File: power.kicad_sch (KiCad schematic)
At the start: 56 parts, among them J11 Conn_01x02_Pin, J13 Conn_01x02_Pin, J14 Conn_01x02_Pin, J15 Conn_01x02_Pin, J8 Conn_01x02_Pin, U10 MAX4995AAUT, U11 MAX4995AAUT, U35 MAX4995AAUT, U36 TPS7A5201QRGRRQ1, U4 TPSM828302ARDSR, U6 STWD100NYWY3F, U8 MP5073GG-P, U9 MAX4995AAUT

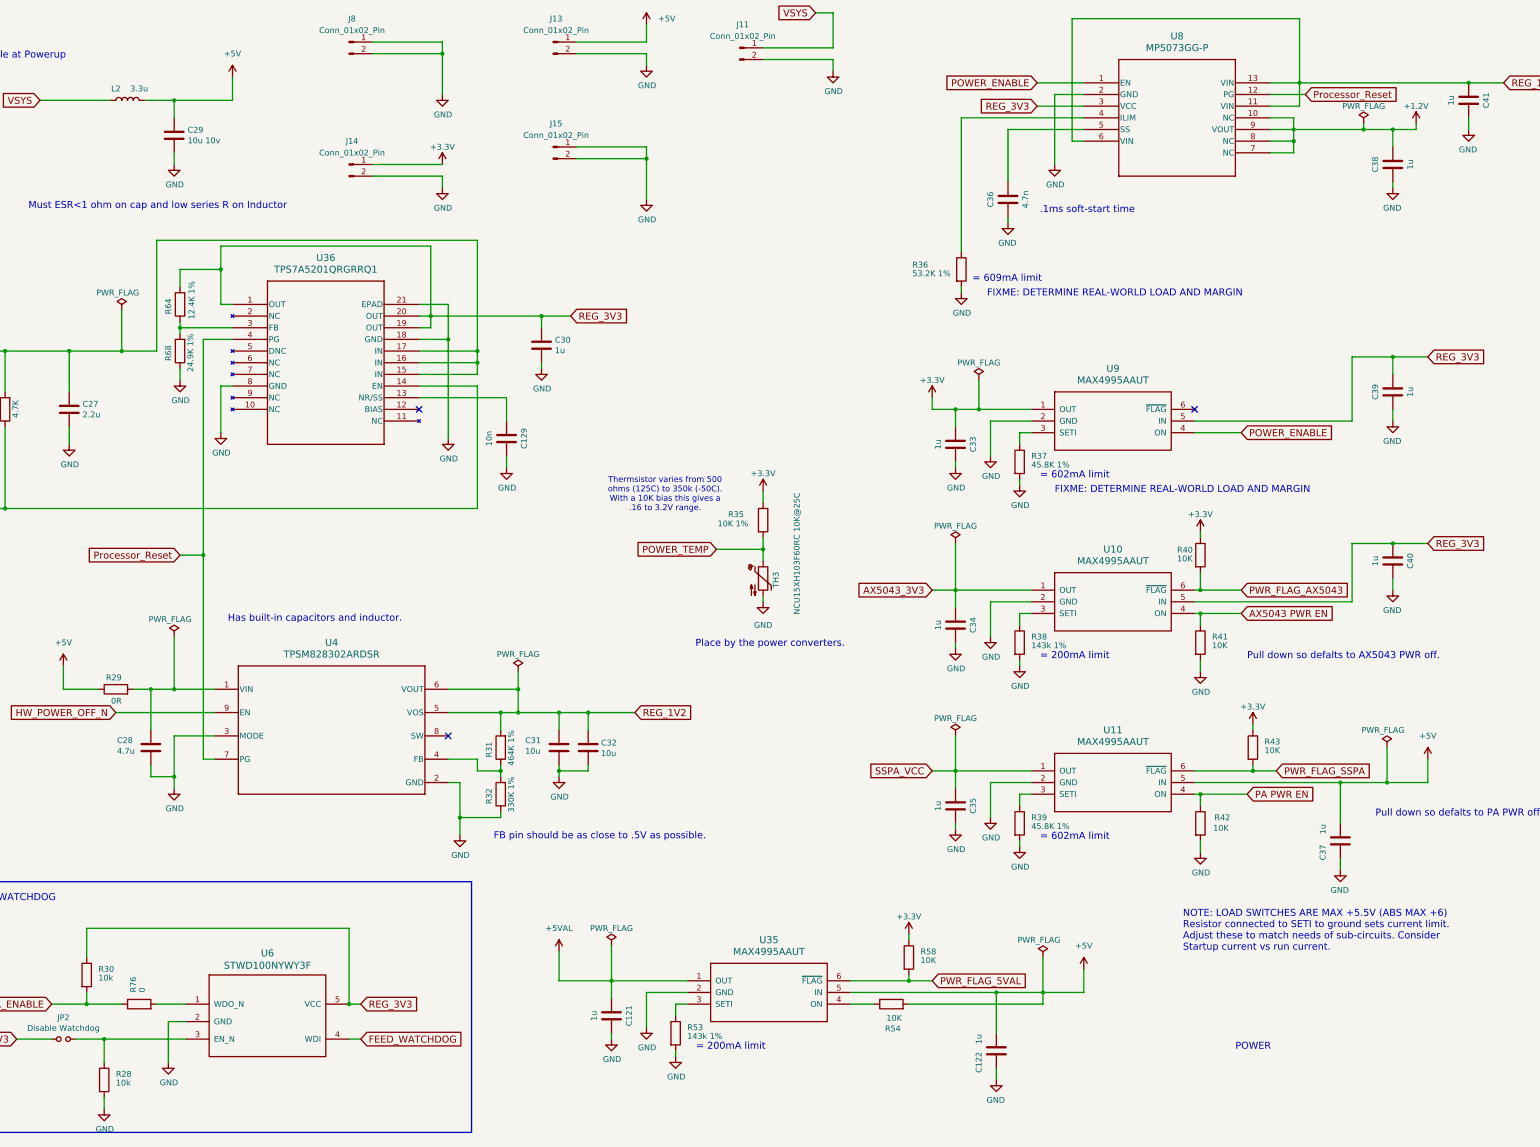
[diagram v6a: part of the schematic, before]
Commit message: Lots of updates to ease manufacturing
Component changes, changes in the formatting of the values, etc.

Signed-off-by: Corey Minyard <corey@minyard.net>
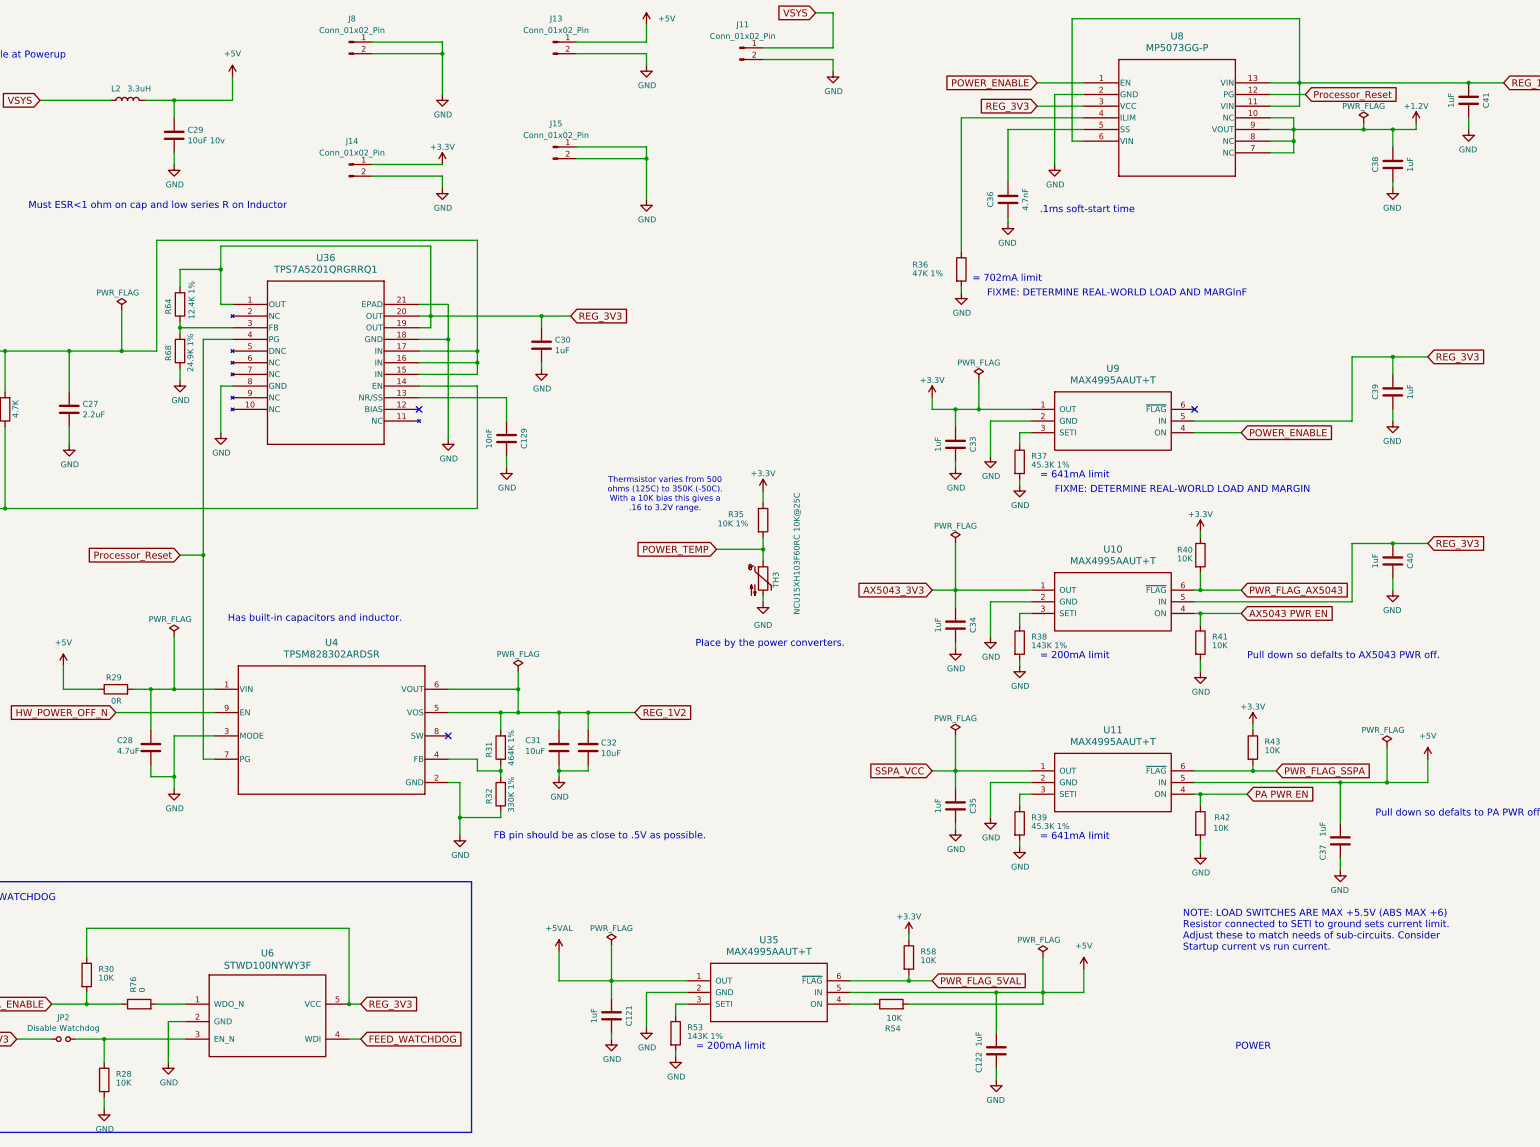
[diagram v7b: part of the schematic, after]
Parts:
- C121, C122, C30, C33, C34, C35, C37, C38, C39, C40, C41: value 1u -> 1uF
- C129: value 10n -> 10nF
- C27: value 2.2u -> 2.2uF
- C28: value 4.7u -> 4.7uF
- C29: value 10u 10v -> 10uF 10v
- C31, C32: value 10u -> 10uF
- C36: value 4.7n -> 4.7nF
- L2: value 3.3u -> 3.3uH
- R28, R30: value 10k -> 10K
- R36: value 53.2K 1% -> 47K 1%
- R37, R39: value 45.8K 1% -> 45.3K 1%
- R38, R53: value 143k 1% -> 143K 1%
- U10, U11, U35, U9: value MAX4995AAUT -> MAX4995AAUT+T
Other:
- note added: "= 641mA limit"
- note added: "= 702mA limit"
- note added: "FIXME: DETERMINE REAL-WORLD LOAD AND MARGInF"
- note added: "Thermsistor varies from 500 ohms (125C) to 350K (-50C). With a 10K bias this gives a .16 to 3.2V range."
- note removed: "= 602mA limit"
- note removed: "= 609mA limit"
- note removed: "Thermsistor varies from 500 ohms (125C) to 350k (-50C). With a 10K bias this gives a .16 to 3.2V range."
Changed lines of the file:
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@@
 		)
 	)
-	(text "Thermsistor varies from 500\nohms (125C) to 350k (-50C).\nWith a 10K bias this gives a\n.16 to 3.2V range."
+	(text "Thermsistor varies from 500\nohms (125C) to 350K (-50C).\nWith a 10K bias this gives a\n.16 to 3.2V range."
 		(exclude_from_sim no)
 		(at 209.804 123.952 0)
@@
 		)
 	)
-	(text "FIXME: DETERMINE REAL-WORLD LOAD AND MARGIN"
+	(text "FIXME: DETERMINE REAL-WORLD LOAD AND MARGInF"
 		(exclude_from_sim no)
 		(at 279.908 81.026 0)
@@
 		)
 	)
-	(text "= 602mA limit"
+	(text "= 641mA limit"
 		(exclude_from_sim no)
 		(at 291.465 120.65 0)
@@
 		)
 	)
-	(text "= 609mA limit"
+	(text "= 702mA limit"
 		(exclude_from_sim no)
 		(at 276.733 77.851 0)
@@
 		)
 	)
-	(text "= 602mA limit"
+	(text "= 641mA limit"
 		(exclude_from_sim no)
 		(at 291.465 199.39 0)
@@
 			)
 		)
-		(property "Value" "1u"
+		(property "Value" "1uF"
 			(at 185.801 92.583 0)
 			(effects
@@
 			)
 		)
-		(property "Value" "2.2u"
+		(property "Value" "2.2uF"
 			(at 82.931 106.553 0)
 			(effects
@@
 			)
 		)
-		(property "Value" "1u"
+		(property "Value" "1uF"
 			(at 364.49 138.43 90)
 			(effects
@@
 			)
 		)
-		(property "Value" "1u"
+		(property "Value" "1uF"
 			(at 353.06 196.85 90)
 			(effects
@@
 			)
 		)
-		(property "Value" "143k 1%"
+		(property "Value" "143K 1%"
 			(at 289.56 156.845 0)
 			(effects
@@
 			)
 		)
-		(property "Value" "45.8K 1%"
+		(property "Value" "45.3K 1%"
 			(at 289.56 196.215 0)
 			(effects
@@
 			)
 		)
-		(property "Value" "1u"
+		(property "Value" "1uF"
 			(at 269.24 152.4 90)
 			(effects
@@
 			)
 		)
-		(property "Value" "1u"
+		(property "Value" "1uF"
 			(at 269.24 191.77 90)
 			(effects
@@
 			)
 		)
-		(property "Value" "1u"
+		(property "Value" "1uF"
 			(at 372.11 101.6 90)
 			(effects
@@
 			)
 		)
-		(property "Value" "1u"
+		(property "Value" "1uF"
 			(at 269.24 113.03 90)
 			(effects
@@
 			)
 		)
-		(property "Value" "45.8K 1%"
+		(property "Value" "45.3K 1%"
 			(at 289.56 117.475 0)
 			(effects
@@
 			)
 		)
-		(property "Value" "1u"
+		(property "Value" "1uF"
 			(at 381 38.1 90)
 			(effects
@@
 			)
 		)
-		(property "Value" "1u"
+		(property "Value" "1uF"
 			(at 372.11 52.07 90)
 			(effects
@@
 			)
 		)
-		(property "Value" "53.2K 1%"
+		(property "Value" "47K 1%"
 			(at 263.652 75.819 0)
 			(effects
@@
 			)
 		)
-		(property "Value" "10k"
+		(property "Value" "10K"
 			(at 86.36 229.235 0)
 			(effects
@@
 			)
 		)
-		(property "Value" "10k"
+		(property "Value" "10K"
 			(at 90.17 252.095 0)
 			(effects
@@
 			)
 		)
-		(property "Value" "10u"
+		(property "Value" "10uF"
 			(at 195.834 180.34 0)
 			(effects
@@
 			)
 		)
-		(property "Value" "10n"
+		(property "Value" "10nF"
 			(at 171.45 111.76 90)
 			(effects
@@
 			)
 		)
-		(property "Value" "3.3u"
+		(property "Value" "3.3uH"
 			(at 95.25 35.56 90)
 			(effects
@@
 			)
 		)
-		(property "Value" "10u 10v"
+		(property "Value" "10uF 10v"
 			(at 105.791 46.863 0)
 			(effects
@@
 			)
 		)
-		(property "Value" "4.7u"
+		(property "Value" "4.7uF"
 			(at 90.424 179.832 0)
 			(effects
@@
 			)
 		)
-		(property "Value" "MAX4995AAUT"
+		(property "Value" "MAX4995AAUT+T"
 			(at 307.34 177.8 0)
 			(effects
@@
 			)
 		)
-		(property "Value" "MAX4995AAUT"
+		(property "Value" "MAX4995AAUT+T"
 			(at 307.34 138.43 0)
 			(effects
@@
 			)
 		)
-		(property "Value" "MAX4995AAUT"
+		(property "Value" "MAX4995AAUT+T"
 			(at 307.34 99.06 0)
 			(effects
@@
 			)
 		)
-		(property "Value" "1u"
+		(property "Value" "1uF"
 			(at 194.31 237.49 90)
 			(effects
@@
 			)
 		)
-		(property "Value" "1u"
+		(property "Value" "1uF"
 			(at 278.13 242.57 90)
 			(effects
@@
 			)
 		)
-		(property "Value" "MAX4995AAUT"
+		(property "Value" "MAX4995AAUT+T"
 			(at 232.41 223.52 0)
 			(effects
@@
 			)
 		)
-		(property "Value" "10u"
+		(property "Value" "10uF"
 			(at 179.324 179.832 0)
 			(effects
@@
 			)
 		)
-		(property "Value" "143k 1%"
+		(property "Value" "143K 1%"
 			(at 214.63 241.935 0)
 			(effects
@@
 			)
 		)
-		(property "Value" "4.7n"
+		(property "Value" "4.7nF"
 			(at 288.29 59.69 90)
 			(effects

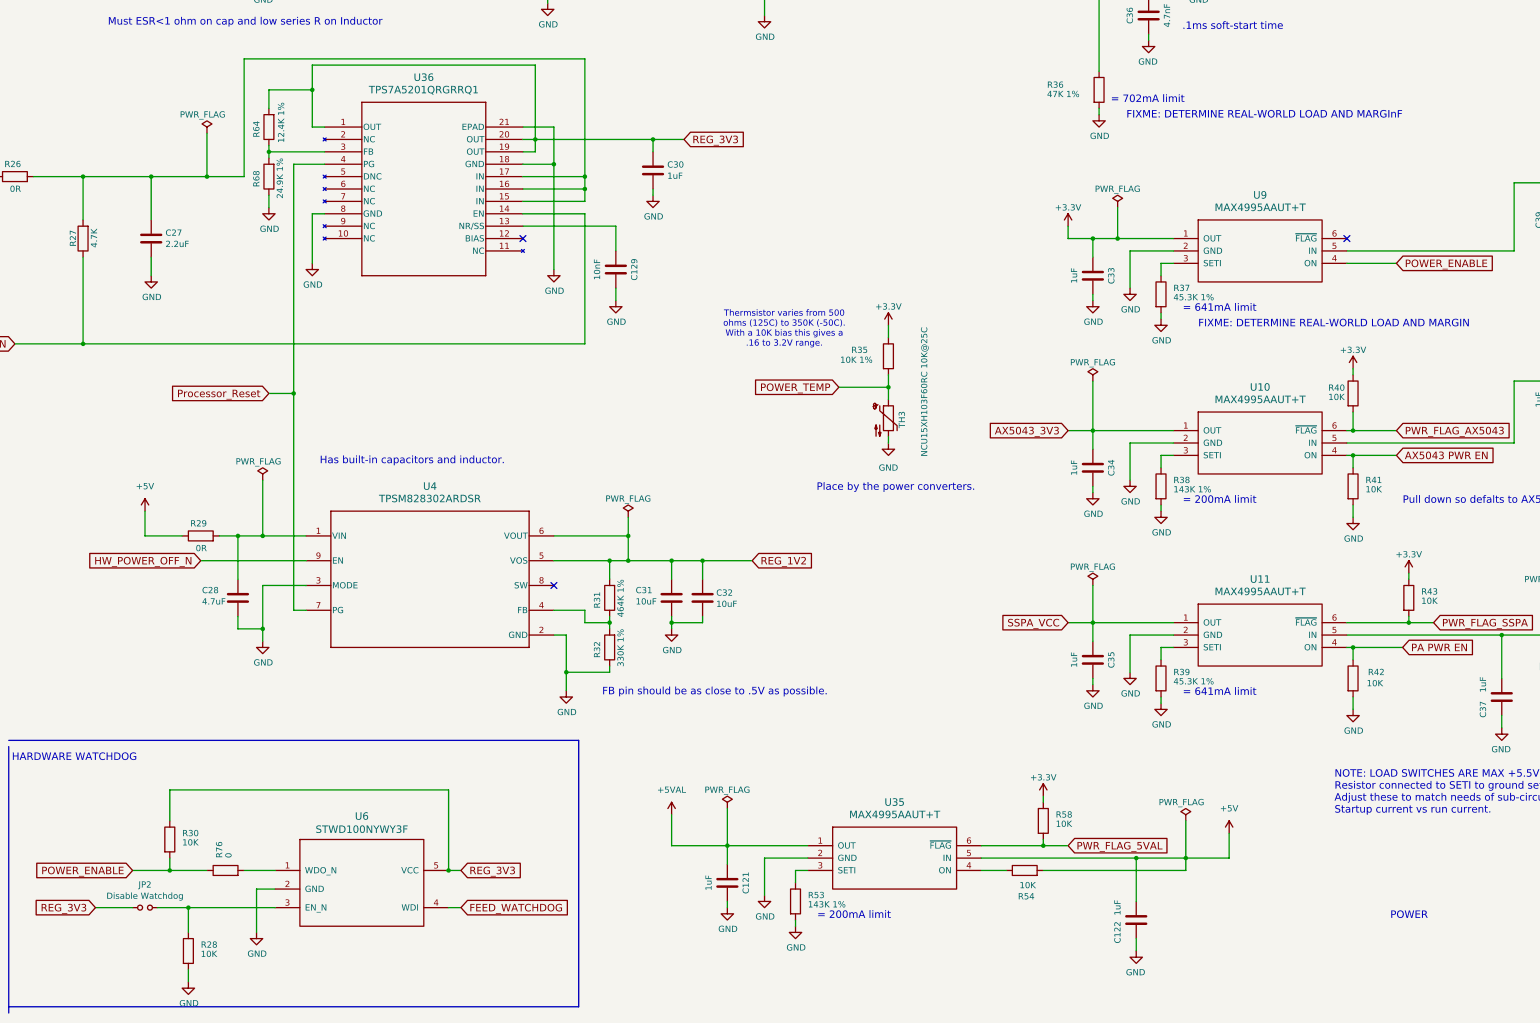
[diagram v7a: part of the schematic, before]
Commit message: Update all resistors to have an ohm symbol
Make it more clean in the BOM what they are.

Signed-off-by: Corey Minyard <corey@minyard.net>
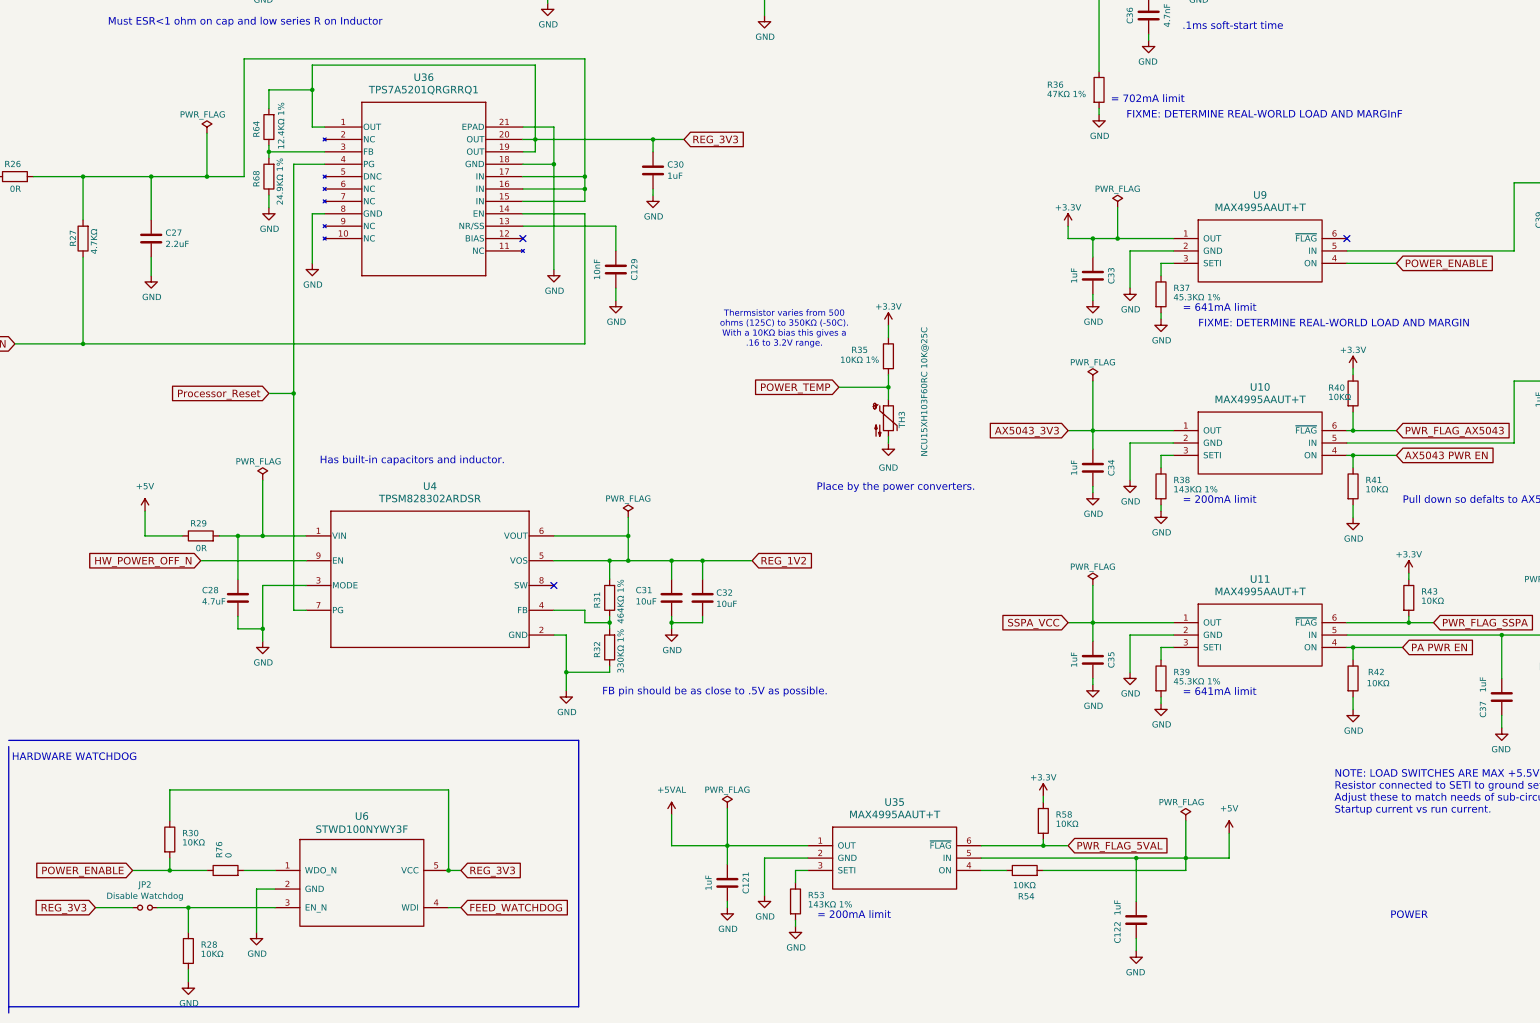
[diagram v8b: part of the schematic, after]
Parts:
- R27: value 4.7K -> 4.7KΩ
- R28, R30, R40, R41, R42, R43, R54, R58: value 10K -> 10KΩ
- R31: value 464K 1% -> 464KΩ 1%
- R32: value 330K 1% -> 330KΩ 1%
- R35: value 10K 1% -> 10KΩ 1%
- R36: value 47K 1% -> 47KΩ 1%
- R37, R39: value 45.3K 1% -> 45.3KΩ 1%
- R38, R53: value 143K 1% -> 143KΩ 1%
- R64: value 12.4K 1% -> 12.4KΩ 1%
- R68: value 24.9K 1% -> 24.9KΩ 1%
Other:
- note added: "Thermsistor varies from 500 ohms (125C) to 350KΩ (-50C). With a 10KΩ bias this gives a .16 to 3.2V range."
- note removed: "Thermsistor varies from 500 ohms (125C) to 350K (-50C). With a 10K bias this gives a .16 to 3.2V range."
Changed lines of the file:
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@@
 		)
 	)
-	(text "Thermsistor varies from 500\nohms (125C) to 350K (-50C).\nWith a 10K bias this gives a\n.16 to 3.2V range."
+	(text "Thermsistor varies from 500\nohms (125C) to 350KΩ (-50C).\nWith a 10KΩ bias this gives a\n.16 to 3.2V range."
 		(exclude_from_sim no)
 		(at 209.804 123.952 0)
@@
 			)
 		)
-		(property "Value" "143K 1%"
+		(property "Value" "143KΩ 1%"
 			(at 289.56 156.845 0)
 			(effects
@@
 			)
 		)
-		(property "Value" "45.3K 1%"
+		(property "Value" "45.3KΩ 1%"
 			(at 289.56 196.215 0)
 			(effects
@@
 			)
 		)
-		(property "Value" "45.3K 1%"
+		(property "Value" "45.3KΩ 1%"
 			(at 289.56 117.475 0)
 			(effects
@@
 			)
 		)
-		(property "Value" "47K 1%"
+		(property "Value" "47KΩ 1%"
 			(at 263.652 75.819 0)
 			(effects
@@
 			)
 		)
-		(property "Value" "10K"
+		(property "Value" "10KΩ"
 			(at 86.36 229.235 0)
 			(effects
@@
 			)
 		)
-		(property "Value" "10K"
+		(property "Value" "10KΩ"
 			(at 90.17 252.095 0)
 			(effects
@@
 			)
 		)
-		(property "Value" "10K"
+		(property "Value" "10KΩ"
 			(at 328.93 156.845 0)
 			(effects
@@
 			)
 		)
-		(property "Value" "10K"
+		(property "Value" "10KΩ"
 			(at 329.184 196.596 0)
 			(effects
@@
 			)
 		)
-		(property "Value" "4.7K"
+		(property "Value" "4.7KΩ"
 			(at 68.326 103.378 90)
 			(effects
@@
 			)
 		)
-		(property "Value" "464K 1%"
+		(property "Value" "464KΩ 1%"
 			(at 176.276 175.26 90)
 			(effects
@@
 			)
 		)
-		(property "Value" "10K 1%"
+		(property "Value" "10KΩ 1%"
 			(at 221.234 130.302 0)
 			(effects
@@
 			)
 		)
-		(property "Value" "10K"
+		(property "Value" "10KΩ"
 			(at 261.366 237.998 90)
 			(effects
@@
 			)
 		)
-		(property "Value" "10K"
+		(property "Value" "10KΩ"
 			(at 321.31 137.922 0)
 			(effects
@@
 			)
 		)
-		(property "Value" "12.4K 1%"
+		(property "Value" "12.4KΩ 1%"
 			(at 106.68 77.47 90)
 			(effects
@@
 			)
 		)
-		(property "Value" "330K 1%"
+		(property "Value" "330KΩ 1%"
 			(at 176.276 185.42 90)
 			(effects
@@
 			)
 		)
-		(property "Value" "10K"
+		(property "Value" "10KΩ"
 			(at 265.43 225.425 0)
 			(effects
@@
 			)
 		)
-		(property "Value" "24.9K 1%"
+		(property "Value" "24.9KΩ 1%"
 			(at 106.426 88.9 90)
 			(effects
@@
 			)
 		)
-		(property "Value" "10K"
+		(property "Value" "10KΩ"
 			(at 340.36 179.705 0)
 			(effects
@@
 			)
 		)
-		(property "Value" "143K 1%"
+		(property "Value" "143KΩ 1%"
 			(at 214.63 241.935 0)
 			(effects
